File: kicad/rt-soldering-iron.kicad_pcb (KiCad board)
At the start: 2 copper layers, 74.9 x 20.3 mm, 104 parts, among them J1 IRON_TIP, J2 BARREL_JACK, J3 CONN_01X04, Q1 SIA483DJ-T1-GE3, Q2 FDG6301N_F085, Q3 MMBT3904, Q4 MMBT3906WT1G, Q5 FDG6301N_F085, Q6 MMBT3906WT1G, Q7 FDG6301N_F085, SW1 SPST, SW2 SPST, U1 ACS711xEX, U2 MCP6V71U, U3 AP3211, U4 STM32F031G, U5 SSD1306-OLED-I2C, U6 MMA8652FC, U7 TL431, U8 TLV1701

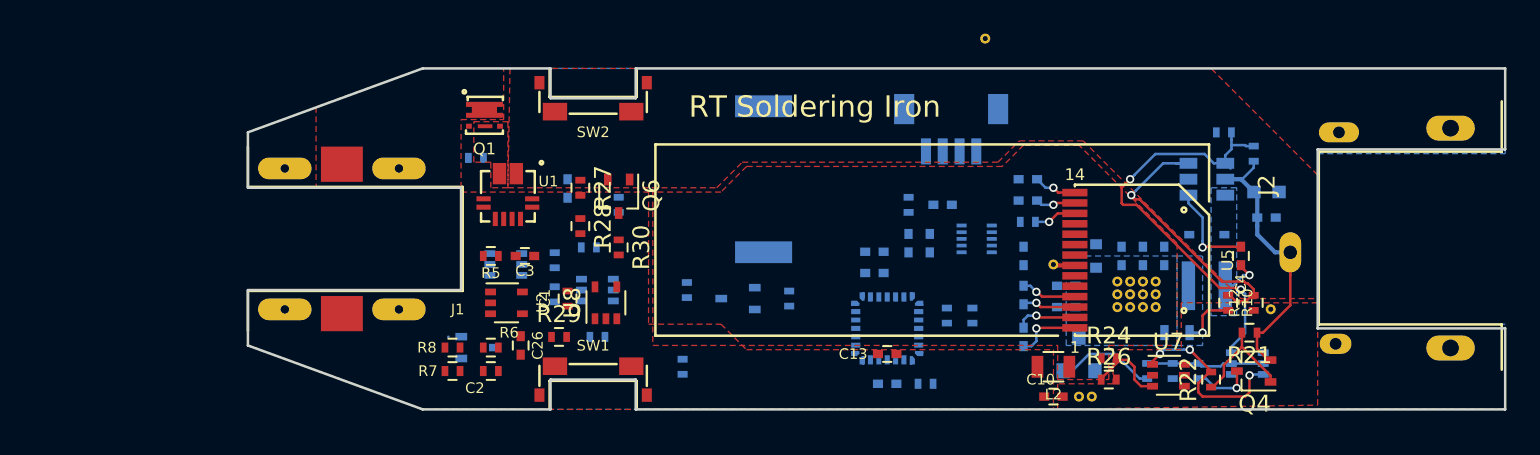
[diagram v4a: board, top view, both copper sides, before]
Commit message: Completed initial routing
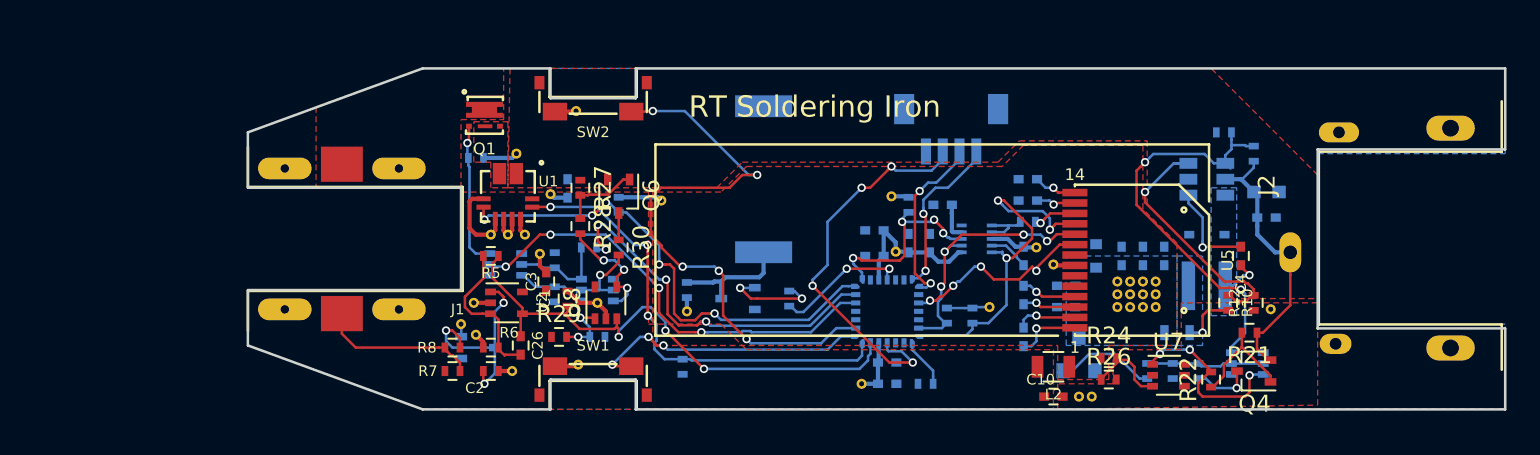
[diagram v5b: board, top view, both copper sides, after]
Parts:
- removed the REF** at (160.5, 84.6)
- added REF**: 1PIN-VIA, rt-soldering-iron:1PIN-VIA, F.Cu at (134.6, 93.9)
- added REF**: 1PIN-VIA, rt-soldering-iron:1PIN-VIA, F.Cu at (155.2, 97.3)
- added REF**: 1PIN-VIA, rt-soldering-iron:1PIN-VIA, F.Cu at (136.1, 88.9)
- added REF**: 1PIN-VIA, rt-soldering-iron:1PIN-VIA, F.Cu at (130.0, 100.3)
- added REF**: 1PIN-VIA, rt-soldering-iron:1PIN-VIA, F.Cu at (137.4, 100.3)
- added REF**: 1PIN-VIA, rt-soldering-iron:1PIN-VIA, F.Cu at (133.1, 96.3)
- added REF**: 1PIN-VIA, rt-soldering-iron:1PIN-VIA, F.Cu at (131.1, 96.3)
- added REF**: 1PIN-VIA, rt-soldering-iron:1PIN-VIA, F.Cu at (132.1, 96.3)
- added REF**: 1PIN-VIA, rt-soldering-iron:1PIN-VIA, F.Cu at (132.3, 104.4)
- added REF**: 1PIN-VIA, rt-soldering-iron:1PIN-VIA, F.Cu at (130.2, 102.2)
- added REF**: 1PIN-VIA, rt-soldering-iron:1PIN-VIA, F.Cu at (136.3, 104.0)
- added REF**: 1PIN-VIA, rt-soldering-iron:1PIN-VIA, F.Cu at (134.0, 97.4)
- added REF**: 1PIN-VIA, rt-soldering-iron:1PIN-VIA, F.Cu at (141.2, 94.2)
- added REF**: 1PIN-VIA, rt-soldering-iron:1PIN-VIA, F.Cu at (132.6, 91.4)
- added REF**: 1PIN-VIA, rt-soldering-iron:1PIN-VIA, F.Cu at (129.3, 101.6)
- added REF**: 1PIN-VIA, rt-soldering-iron:1PIN-VIA, F.Cu at (153.2, 105.2)
- added REF**: 1PIN-VIA, rt-soldering-iron:1PIN-VIA, F.Cu at (160.8, 100.6)
- added REF**: 1PIN-VIA, rt-soldering-iron:1PIN-VIA, F.Cu at (163.6, 97.0)
- added REF**: 1PIN-VIA, rt-soldering-iron:1PIN-VIA, F.Cu at (154.9, 94.0)
- added REF**: 1PIN-VIA, rt-soldering-iron:1PIN-VIA, F.Cu at (142.7, 100.8)
- C13: moved to B.Cu
- moved C3 1.98 mm to (134.4, 99.1), turned to 90 degrees
- moved C12 1.27 mm to (153.9, 96.0)
- moved C11 1.02 mm to (153.9, 97.5)
- moved U4 1.02 mm to (154.7, 100.8)
- moved C13 0.51 mm to (154.7, 103.9)
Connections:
- SW2 pad 1: GND -> /Digital Control/SW_B
- SW2 pad 2: /Digital Control/SW_B -> GND
- U4 pad 12: Net-(U4-Pad12) -> /Analog Frontend/HEATER_LATCH_RESET
- U4 pad 25: /Analog Frontend/HEATER_LATCH_RESET -> Net-(U4-Pad25)
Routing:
- net /Digital Control/SW_B: track 0.00 -> 35.0 mm, vias 0 -> 5
- net /Analog Frontend/HEATER_SENSE: track 0.00 -> 32.4 mm, vias 0 -> 3
- net /Analog Frontend/~FAULT: track 0.00 -> 29.5 mm, vias 0 -> 5
- net /Analog Frontend/CURRENT_SENSE: track 0.00 -> 27.7 mm, vias 0 -> 3
- net /Analog Frontend/HEATER_LATCH_RESET: track 0.00 -> 26.7 mm, vias 0 -> 4
- net GND: track 1.30 -> 24.8 mm
- net /Digital Control/~STM32_RESET: track 0.00 -> 23.4 mm, vias 0 -> 4
- net /Analog Frontend/HEATER_CTL: track 0.00 -> 22.3 mm, vias 0 -> 4
- net /Digital Control/I2C_SDA: track 0.00 -> 21.2 mm, vias 0 -> 3
- net +3V3: track 0.00 -> 19.0 mm
- net /Digital Control/SW_A: track 0.00 -> 16.9 mm, vias 0 -> 3
- net /Digital Control/I2C_SCL: track 0.00 -> 16.2 mm, vias 0 -> 4
- net /Analog Frontend/OPAMP_SENSE_IN: track 0.00 -> 12.8 mm, vias 0 -> 3
- net /Digital Control/ACC_INT: track 0.00 -> 11.8 mm, vias 0 -> 4
- net /Digital Control/~OLED_RST: track 0.00 -> 11.7 mm, vias 0 -> 4
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
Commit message: Initial silkscreen fixing
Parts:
- moved R33 0.51 mm to (169.7, 104.4)
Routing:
- net /Power Supplies/OVP_LATCH_OUT: track 7.05 -> 7.56 mm
